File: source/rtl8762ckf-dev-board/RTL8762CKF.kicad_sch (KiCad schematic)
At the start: 14 parts, among them U5 RTL8762CKF, Y1 40MHz

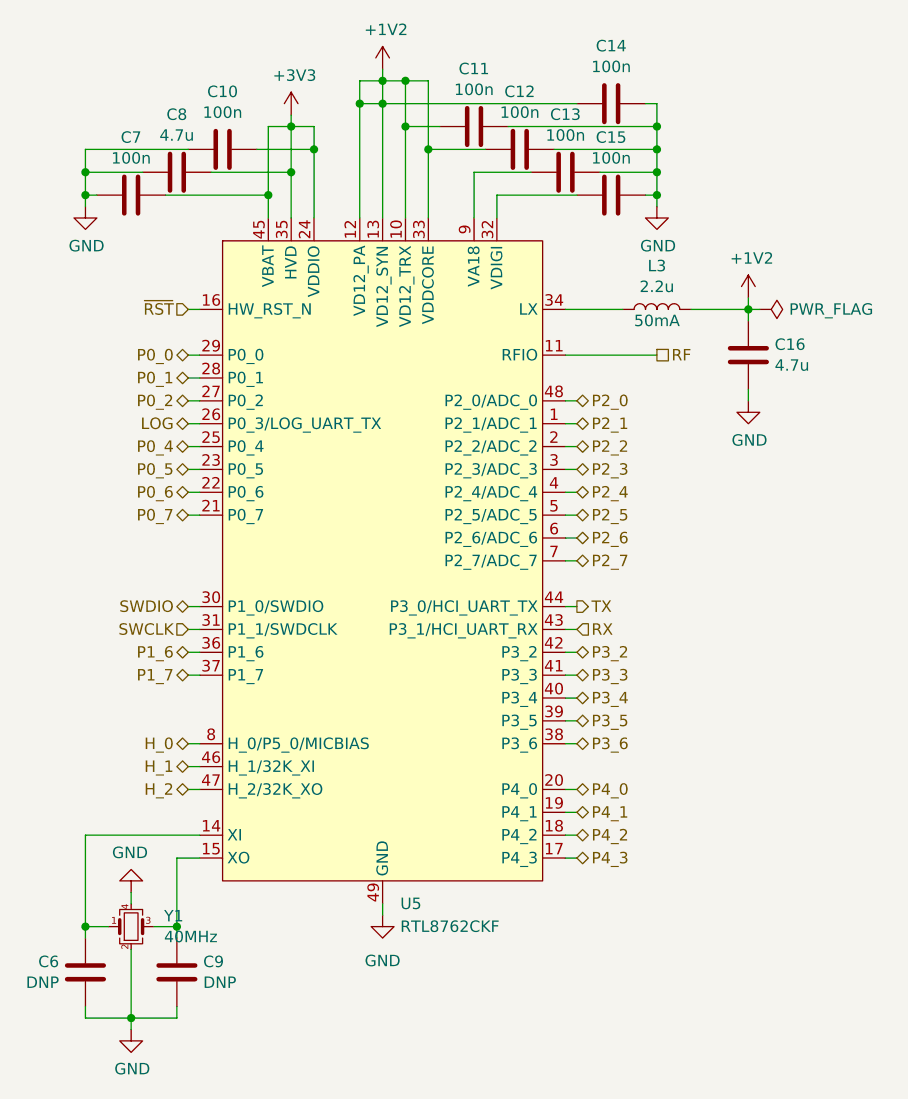
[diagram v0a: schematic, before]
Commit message: implemented pico probe
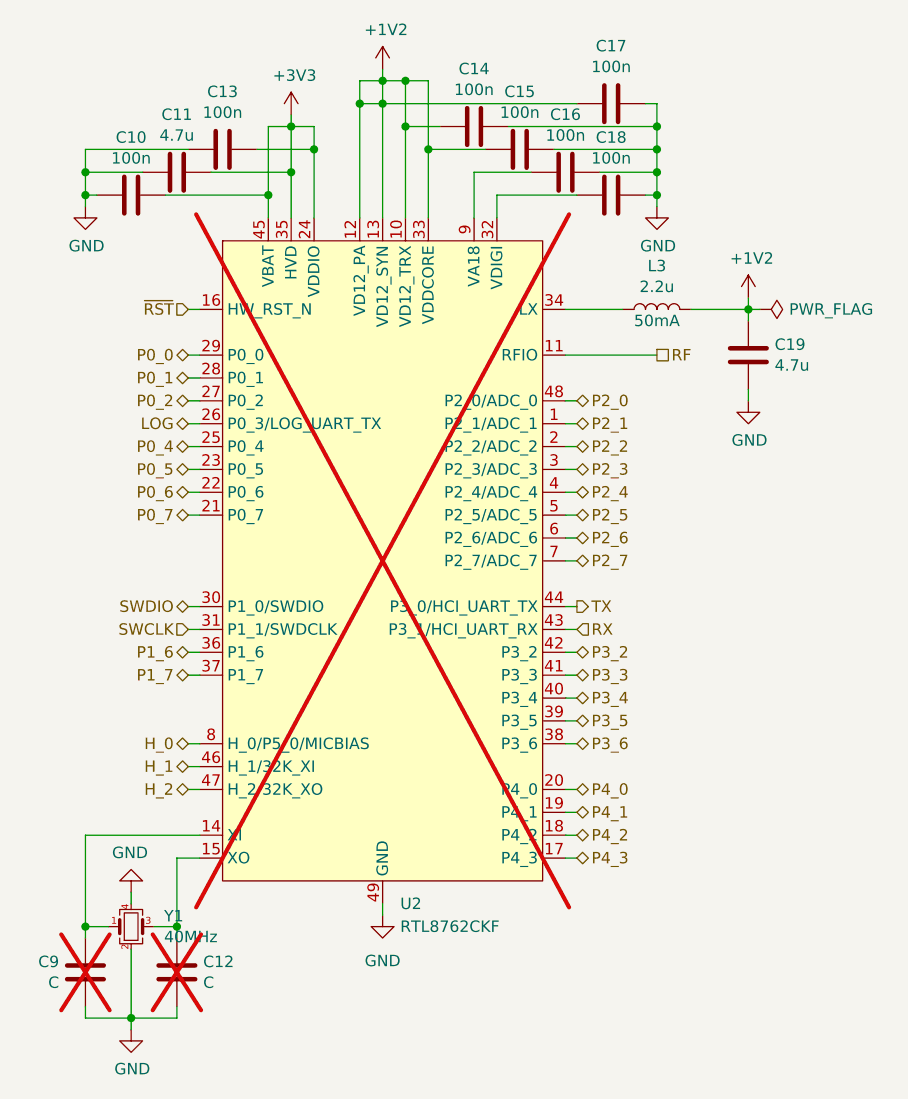
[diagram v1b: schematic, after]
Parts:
- C10: renamed from C7; LCSC C83056 -> C1546; MPN (none) -> 0402CG101J500NT
- C11: renamed from C8; LCSC C2980397 -> C23733; MPN (none) -> CL05A475MP5NRNC
- C12: renamed from C9; value DNP -> C; LCSC DNP -> (none); now not fitted
- C13: renamed from C10; LCSC C83056 -> C1546; MPN (none) -> 0402CG101J500NT
- C14: renamed from C11; LCSC C83056 -> C1546; MPN (none) -> 0402CG101J500NT
- C15: renamed from C12; LCSC C83056 -> C1546; MPN (none) -> 0402CG101J500NT
- C16: renamed from C13; LCSC C83056 -> C1546; MPN (none) -> 0402CG101J500NT
- C17: renamed from C14; LCSC C83056 -> C1546; MPN (none) -> 0402CG101J500NT
- C18: renamed from C15; LCSC C83056 -> C1546; MPN (none) -> 0402CG101J500NT
- C19: renamed from C16; LCSC C2980397 -> C23733; MPN (none) -> CL05A475MP5NRNC
- C9: renamed from C6; value DNP -> C; LCSC DNP -> (none); now not fitted
- L3: LCSC C365953 -> C12530; MPN (none) -> CL05A225MQ5NSNC
- U2: renamed from U5; now not fitted
- Y1: MPN (none) -> 9S40000048

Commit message: change part number of RTL8762C power inductor; closes #2
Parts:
- L3: footprint Inductor_SMD:L_0603_1608Metric -> Inductor_SMD:L_0805_2012Metric; LCSC C12530 -> C394950; MPN CL05A225MQ5NSNC -> CMH160808B2R2MT
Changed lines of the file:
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@@
       (effects (font (size 1.27 1.27)))
     )
-    (property "Footprint" "Inductor_SMD:L_0603_1608Metric" (at 157.48 63.5 0)
+    (property "Footprint" "Inductor_SMD:L_0805_2012Metric" (at 157.48 63.5 0)
       (effects (font (size 1.27 1.27)) hide)
     )
-    (property "Datasheet" "https://datasheet.lcsc.com/lcsc/1912111437_Chilisin-Elec-CPY160808T-2R2M-NP_C365953.pdf" (at 157.48 63.5 0)
+    (property "Datasheet" "https://datasheet.lcsc.com/lcsc/2302231130_FH--Guangdong-Fenghua-Advanced-Tech-CMP160808UE2R2MT_C2961322.pdf" (at 157.48 63.5 0)
       (effects (font (size 1.27 1.27)) hide)
     )
-    (property "LCSC" "C12530" (at 157.48 63.5 90)
+    (property "LCSC" "C394950" (at 157.48 63.5 90)
       (effects (font (size 1.27 1.27)) hide)
     )
@@
       (effects (font (size 1.27 1.27)))
     )
-    (property "MPN" "CL05A225MQ5NSNC" (at 157.48 63.5 0)
+    (property "MPN" "CMH160808B2R2MT" (at 157.48 63.5 0)
       (effects (font (size 1.27 1.27)) hide)
     )
